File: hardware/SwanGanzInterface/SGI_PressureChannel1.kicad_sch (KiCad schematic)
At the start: 20 parts, among them J6 Conn_01x04_Pin, U10 INA122D, U11 OPA2350

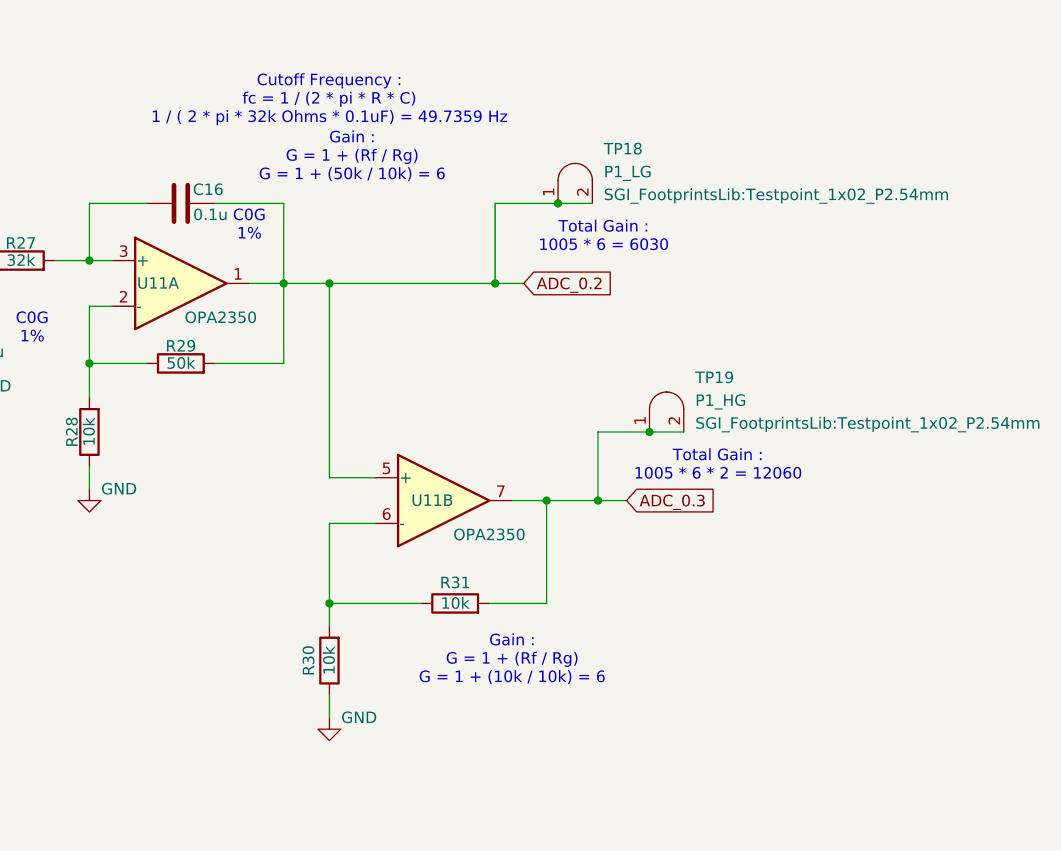
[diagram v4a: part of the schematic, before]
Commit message: Updated Pressure Gain
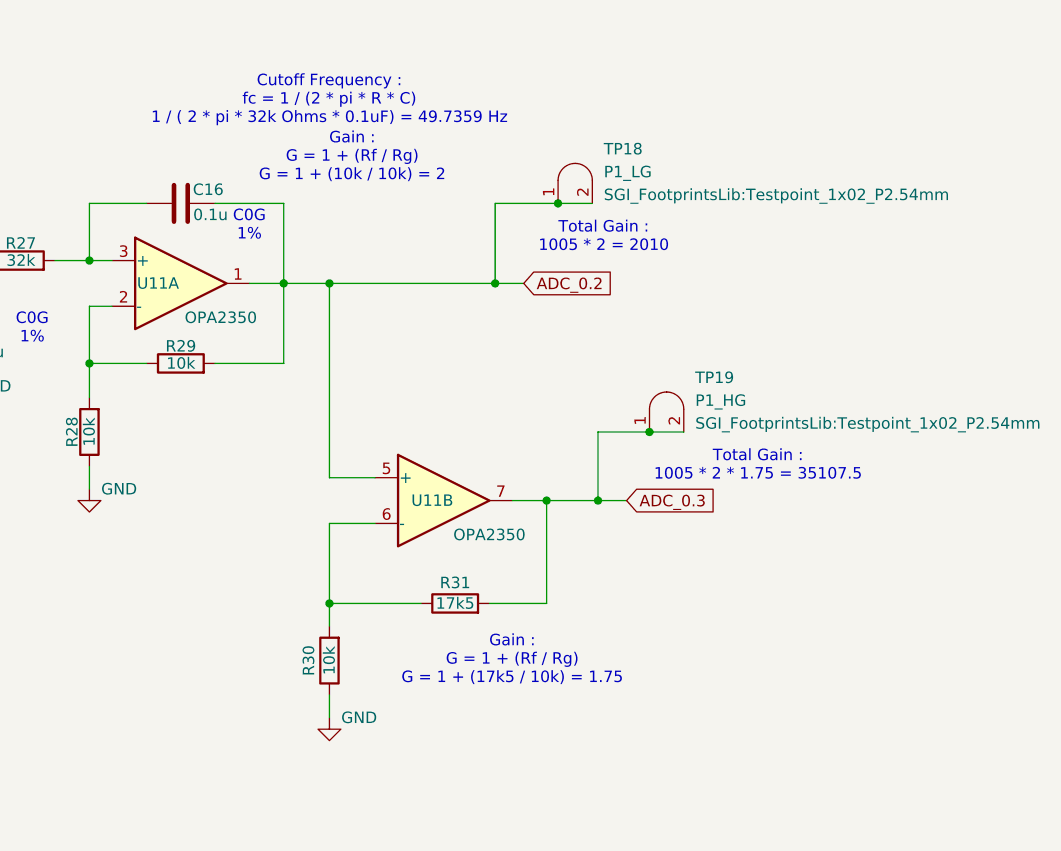
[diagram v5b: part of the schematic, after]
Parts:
- R29: value 50k -> 10k
- R31: value 10k -> 17k5
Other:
- note added: "Gain : G = 1 + (Rf / Rg) G = 1 + (10k / 10k) = 2"
- note added: "Gain : G = 1 + (Rf / Rg) G = 1 + (17k5 / 10k) = 1.75"
- note added: "Total Gain : 1005 * 2 * 1.75 = 35107.5"
- note added: "Total Gain : 1005 * 2 = 2010"
- note removed: "Gain : G = 1 + (Rf / Rg) G = 1 + (10k / 10k) = 6"
- note removed: "Gain : G = 1 + (Rf / Rg) G = 1 + (50k / 10k) = 6"
- note removed: "Total Gain : 1005 * 6 * 2 = 12060"
- note removed: "Total Gain : 1005 * 6 = 6030"
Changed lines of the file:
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@@
 		(comment 3 "Faculty Mentor - Dr. Valvano")
 	)
-	(text "Gain :\nG = 1 + (Rf / Rg)\nG = 1 + (10k / 10k) = 6"
+	(text "Gain :\nG = 1 + (Rf / Rg)\nG = 1 + (17k5 / 10k) = 1.75"
 		(exclude_from_sim no)
 		(at 166.37 106.68 0)
@@
 		)
 	)
-	(text "Total Gain :\n1005 * 6 = 6030"
+	(text "Total Gain :\n1005 * 2 = 2010"
 		(exclude_from_sim no)
 		(at 176.53 59.69 0)
@@
 		)
 	)
-	(text "Gain :\nG = 1 + (Rf / Rg)\nG = 1 + (50k / 10k) = 6"
+	(text "Gain :\nG = 1 + (Rf / Rg)\nG = 1 + (10k / 10k) = 2"
 		(exclude_from_sim no)
 		(at 148.59 50.8 0)
@@
 		)
 	)
-	(text "Total Gain :\n1005 * 6 * 2 = 12060"
-		(exclude_from_sim no)
-		(at 189.23 85.09 0)
+	(text "Total Gain :\n1005 * 2 * 1.75 = 35107.5"
+		(exclude_from_sim no)
+		(at 193.675 85.09 0)
 		(effects
 			(font
@@
 			)
 		)
-		(property "Value" "50k"
+		(property "Value" "10k"
 			(at 129.54 73.66 90)
 			(effects
@@
 			)
 		)
-		(property "Value" "10k"
+		(property "Value" "17k5"
 			(at 160.02 100.33 90)
 			(effects

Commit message: Started Routing
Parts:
- removed TP16, TP17: TP, SGI_FootprintsLib:Testpoint_1x02_P2.54mm, symbol SGI_SymbolLib:Testpoint
- J4: footprint (none) -> SGI_FootprintsLib:Pressure_Connector
- TP15: value TP -> P1_InstOut
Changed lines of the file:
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@@
 	)
 	(junction
-		(at 45.72 134.62)
-		(diameter 0)
-		(color 0 0 0 0)
-	)
-	(junction
 		(at 40.64 59.69)
 		(diameter 0)
@@
 	)
 	(junction
-		(at 45.72 142.24)
-		(diameter 0)
-		(color 0 0 0 0)
-	)
-	(junction
 		(at 164.465 64.77)
 		(diameter 0)
@@
 	(wire
 		(pts
-			(xy 45.72 134.62) (xy 49.53 134.62)
-		)
-		(stroke
-			(width 0)
-			(type default)
-		)
-	)
-	(wire
-		(pts
 			(xy 275.59 49.53) (xy 262.89 49.53)
 		)
@@
 	(wire
 		(pts
-			(xy 39.37 142.24) (xy 45.72 142.24)
-		)
-		(stroke
-			(width 0)
-			(type default)
-		)
-	)
-	(wire
-		(pts
 			(xy 146.05 86.36) (xy 146.05 64.77)
 		)
@@
 	(wire
 		(pts
-			(xy 40.64 134.62) (xy 45.72 134.62)
-		)
-		(stroke
-			(width 0)
-			(type default)
-		)
-	)
-	(wire
-		(pts
 			(xy 275.59 34.29) (xy 275.59 26.67)
 		)
@@
 	(wire
 		(pts
-			(xy 45.72 142.24) (xy 49.53 142.24)
-		)
-		(stroke
-			(width 0)
-			(type default)
-		)
-	)
-	(wire
-		(pts
 			(xy 140.97 64.77) (xy 137.16 64.77)
 		)
@@
 		)
 	)
-	(global_label "Pres1AmpOut_LowGain"
-		(shape input)
-		(at 40.64 134.62 180)
-		(fields_autoplaced yes)
-		(effects
-			(font
-				(size 1.27 1.27)
-			)
-			(justify right)
-		)
-		(property "Intersheetrefs" "${INTERSHEET_REFS}"
-			(at 16.4883 134.62 0)
-			(effects
-				(font
-					(size 1.27 1.27)
-				)
-				(justify right)
-				(hide yes)
-			)
-		)
-	)
 	(global_label "P1__InstrOut"
 		(shape input)
@@
 		)
 	)
-	(global_label "Pres1AmpOut_HighGain"
-		(shape input)
-		(at 39.37 142.24 180)
-		(fields_autoplaced yes)
-		(effects
-			(font
-				(size 1.27 1.27)
-			)
-			(justify right)
-		)
-		(property "Intersheetrefs" "${INTERSHEET_REFS}"
-			(at 14.4926 142.24 0)
-			(effects
-				(font
-					(size 1.27 1.27)
-				)
-				(justify right)
-				(hide yes)
-			)
-		)
-	)
-	(symbol
-		(lib_id "SGI_SymbolLib:Testpoint")
-		(at 47.625 134.62 0)
-		(unit 1)
-		(exclude_from_sim no)
-		(in_bom yes)
-		(on_board yes)
-		(dnp no)
-		(fields_autoplaced yes)
-		(property "Reference" "TP16"
-			(at 51.181 128.5873 0)
-			(effects
-				(font
-					(size 1.27 1.27)
-				)
-				(justify left)
-			)
-		)
-		(property "Value" "TP"
-			(at 51.181 131.1273 0)
-			(effects
-				(font
-					(size 1.27 1.27)
-				)
-				(justify left)
-			)
-		)
-		(property "Footprint" "SGI_FootprintsLib:Testpoint_1x02_P2.54mm"
-			(at 51.181 133.6673 0)
-			(effects
-				(font
-					(size 1.27 1.27)
-				)
-				(justify left)
-			)
-		)
-		(property "Datasheet" "~"
-			(at 47.625 134.62 0)
-			(effects
-				(font
-					(size 1.27 1.27)
-				)
-				(hide yes)
-			)
-		)
-		(property "Description" "Testpoint"
-			(at 47.625 134.62 0)
-			(effects
-				(font
-					(size 1.27 1.27)
-				)
-				(hide yes)
-			)
-		)
-		(pin "2"
-		)
-		(pin "1"
-		)
-		(instances
-			(project "SwanGanzInterface"
-				(path "/4e9a6e30-f660-472b-9696-bea1f34b4545/3d8fa9e7-4833-4941-a955-d778effe3e32"
-					(reference "TP16")
-					(unit 1)
-				)
-			)
-		)
-	)
 	(symbol
 		(lib_id "power:GNDA")
@@
 		(fields_autoplaced yes)
 		(property "Reference" "TP15"
-			(at 51.181 120.9673 0)
+			(at 50.8 120.9673 0)
 			(effects
 				(font
@@
 			)
 		)
-		(property "Value" "TP"
-			(at 51.181 123.5073 0)
+		(property "Value" "P1_InstOut"
+			(at 50.8 123.5073 0)
 			(effects
 				(font
@@
 		)
 		(property "Footprint" "SGI_FootprintsLib:Testpoint_1x02_P2.54mm"
-			(at 51.181 126.0473 0)
+			(at 50.8 126.0473 0)
 			(effects
 				(font
@@
 			)
 		)
-		(property "Footprint" ""
+		(property "Footprint" "SGI_FootprintsLib:Pressure_Connector"
 			(at 24.13 62.23 0)
 			(effects
@@
 	)
 	(symbol
-		(lib_id "SGI_SymbolLib:Testpoint")
-		(at 47.625 142.24 0)
-		(unit 1)
-		(exclude_from_sim no)
-		(in_bom yes)
-		(on_board yes)
-		(dnp no)
-		(fields_autoplaced yes)
-		(property "Reference" "TP17"
-			(at 51.181 136.2073 0)
-			(effects
-				(font
-					(size 1.27 1.27)
-				)
-				(justify left)
-			)
-		)
-		(property "Value" "TP"
-			(at 51.181 138.7473 0)
-			(effects
-				(font
-					(size 1.27 1.27)
-				)
-				(justify left)
-			)
-		)
-		(property "Footprint" "SGI_FootprintsLib:Testpoint_1x02_P2.54mm"
-			(at 51.181 141.2873 0)
-			(effects
-				(font
-					(size 1.27 1.27)
-				)
-				(justify left)
-			)
-		)
-		(property "Datasheet" "~"
-			(at 47.625 142.24 0)
-			(effects
-				(font
-					(size 1.27 1.27)
-				)
-				(hide yes)
-			)
-		)
-		(property "Description" "Testpoint"
-			(at 47.625 142.24 0)
-			(effects
-				(font
-					(size 1.27 1.27)
-				)
-				(hide yes)
-			)
-		)
-		(pin "2"
-		)
-		(pin "1"
-		)
-		(instances
-			(project "SwanGanzInterface"
-				(path "/4e9a6e30-f660-472b-9696-bea1f34b4545/3d8fa9e7-4833-4941-a955-d778effe3e32"
-					(reference "TP17")
-					(unit 1)
-				)
-			)
-		)
-	)
-	(symbol
 		(lib_id "Device:R")
 		(at 97.79 62.23 90)
@@
 			)
 		)
-		(property "Footprint" ""
+		(property "Footprint" "SGI_FootprintsLib:Pressure_Connector"
 			(at 24.13 99.06 0)
 			(effects

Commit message: Reannotated symbols
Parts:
- renumbered J6 to J5, TP15 to TP10, TP18 to TP11, TP19 to TP12
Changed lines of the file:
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@@
 		(on_board yes)
 		(dnp no)
-		(property "Reference" "#PWR059"
+		(property "Reference" "#PWR057"
 			(at 146.05 119.38 0)
 			(effects
@@
 			(project "SwanGanzInterface"
 				(path "/4e9a6e30-f660-472b-9696-bea1f34b4545/3d8fa9e7-4833-4941-a955-d778effe3e32"
-					(reference "#PWR059")
+					(reference "#PWR057")
 					(unit 1)
 				)
@@
 		(dnp no)
 		(fields_autoplaced yes)
-		(property "Reference" "#PWR055"
+		(property "Reference" "#PWR053"
 			(at 74.93 46.99 0)
 			(effects
@@
 			(project "SwanGanzInterface"
 				(path "/4e9a6e30-f660-472b-9696-bea1f34b4545/3d8fa9e7-4833-4941-a955-d778effe3e32"
-					(reference "#PWR055")
+					(reference "#PWR053")
 					(unit 1)
 				)
@@
 		(on_board yes)
 		(dnp no)
-		(property "Reference" "#PWR057"
+		(property "Reference" "#PWR055"
 			(at 105.41 82.55 0)
 			(effects
@@
 			(project "SwanGanzInterface"
 				(path "/4e9a6e30-f660-472b-9696-bea1f34b4545/3d8fa9e7-4833-4941-a955-d778effe3e32"
-					(reference "#PWR057")
+					(reference "#PWR055")
 					(unit 1)
 				)
@@
 		(dnp no)
 		(fields_autoplaced yes)
-		(property "Reference" "J6"
+		(property "Reference" "J5"
 			(at 26.035 177.8 0)
 			(effects
@@
 			(project ""
 				(path "/4e9a6e30-f660-472b-9696-bea1f34b4545/3d8fa9e7-4833-4941-a955-d778effe3e32"
-					(reference "J6")
+					(reference "J5")
 					(unit 1)
 				)
@@
 		(on_board yes)
 		(dnp no)
-		(property "Reference" "#PWR054"
+		(property "Reference" "#PWR052"
 			(at 62.23 88.9 0)
 			(effects
@@
 			(project "SwanGanzInterface"
 				(path "/4e9a6e30-f660-472b-9696-bea1f34b4545/3d8fa9e7-4833-4941-a955-d778effe3e32"
-					(reference "#PWR054")
+					(reference "#PWR052")
 					(unit 1)
 				)
@@
 		(on_board yes)
 		(dnp no)
-		(property "Reference" "#PWR072"
+		(property "Reference" "#PWR049"
 			(at 35.56 199.39 0)
 			(effects
@@
 			(project "SwanGanzInterface"
 				(path "/4e9a6e30-f660-472b-9696-bea1f34b4545/3d8fa9e7-4833-4941-a955-d778effe3e32"
-					(reference "#PWR072")
+					(reference "#PWR049")
 					(unit 1)
 				)
@@
 		(on_board yes)
 		(dnp no)
-		(property "Reference" "#PWR058"
+		(property "Reference" "#PWR056"
 			(at 119.38 93.98 0)
 			(effects
@@
 			(project "SwanGanzInterface"
 				(path "/4e9a6e30-f660-472b-9696-bea1f34b4545/3d8fa9e7-4833-4941-a955-d778effe3e32"
-					(reference "#PWR058")
+					(reference "#PWR056")
 					(unit 1)
 				)
@@
 		(dnp no)
 		(fields_autoplaced yes)
-		(property "Reference" "#PWR061"
+		(property "Reference" "#PWR059"
 			(at 262.89 58.42 0)
 			(effects
@@
 			(project "SwanGanzInterface"
 				(path "/4e9a6e30-f660-472b-9696-bea1f34b4545/3d8fa9e7-4833-4941-a955-d778effe3e32"
-					(reference "#PWR061")
+					(reference "#PWR059")
 					(unit 1)
 				)
@@
 		(dnp no)
 		(fields_autoplaced yes)
-		(property "Reference" "TP15"
+		(property "Reference" "TP10"
 			(at 50.8 120.9673 0)
 			(effects
@@
 			(project "SwanGanzInterface"
 				(path "/4e9a6e30-f660-472b-9696-bea1f34b4545/3d8fa9e7-4833-4941-a955-d778effe3e32"
-					(reference "TP15")
+					(reference "TP10")
 					(unit 1)
 				)
@@
 		(on_board yes)
 		(dnp no)
-		(property "Reference" "#PWR053"
+		(property "Reference" "#PWR051"
 			(at 62.23 39.37 0)
 			(effects
@@
 			(project "SwanGanzInterface"
 				(path "/4e9a6e30-f660-472b-9696-bea1f34b4545/3d8fa9e7-4833-4941-a955-d778effe3e32"
-					(reference "#PWR053")
+					(reference "#PWR051")
 					(unit 1)
 				)
@@
 		(dnp no)
 		(fields_autoplaced yes)
-		(property "Reference" "TP18"
+		(property "Reference" "TP11"
 			(at 176.53 49.8473 0)
 			(effects
@@
 			(project "SwanGanzInterface"
 				(path "/4e9a6e30-f660-472b-9696-bea1f34b4545/3d8fa9e7-4833-4941-a955-d778effe3e32"
-					(reference "TP18")
+					(reference "TP11")
 					(unit 1)
 				)
@@
 		(dnp no)
 		(fields_autoplaced yes)
-		(property "Reference" "TP19"
+		(property "Reference" "TP12"
 			(at 186.69 75.2473 0)
 			(effects
@@
 			(project "SwanGanzInterface"
 				(path "/4e9a6e30-f660-472b-9696-bea1f34b4545/3d8fa9e7-4833-4941-a955-d778effe3e32"
-					(reference "TP19")
+					(reference "TP12")
 					(unit 1)
 				)
@@
 		(on_board yes)
 		(dnp no)
-		(property "Reference" "#PWR052"
+		(property "Reference" "#PWR050"
 			(at 36.83 78.74 0)
 			(effects
@@
 			(project "SwanGanzInterface"
 				(path "/4e9a6e30-f660-472b-9696-bea1f34b4545/3d8fa9e7-4833-4941-a955-d778effe3e32"
-					(reference "#PWR052")
+					(reference "#PWR050")
 					(unit 1)
 				)
@@
 		(on_board yes)
 		(dnp no)
-		(property "Reference" "#PWR056"
+		(property "Reference" "#PWR054"
 			(at 74.93 83.82 0)
 			(effects
@@
 			(project "SwanGanzInterface"
 				(path "/4e9a6e30-f660-472b-9696-bea1f34b4545/3d8fa9e7-4833-4941-a955-d778effe3e32"
-					(reference "#PWR056")
+					(reference "#PWR054")
 					(unit 1)
 				)
@@
 		(on_board yes)
 		(dnp no)
-		(property "Reference" "#PWR060"
+		(property "Reference" "#PWR058"
 			(at 262.89 27.94 0)
 			(effects
@@
 			(project "SwanGanzInterface"
 				(path "/4e9a6e30-f660-472b-9696-bea1f34b4545/3d8fa9e7-4833-4941-a955-d778effe3e32"
-					(reference "#PWR060")
-					(unit 1)
-				)
+					(reference "#PWR058")
+					(unit 1)
+				)

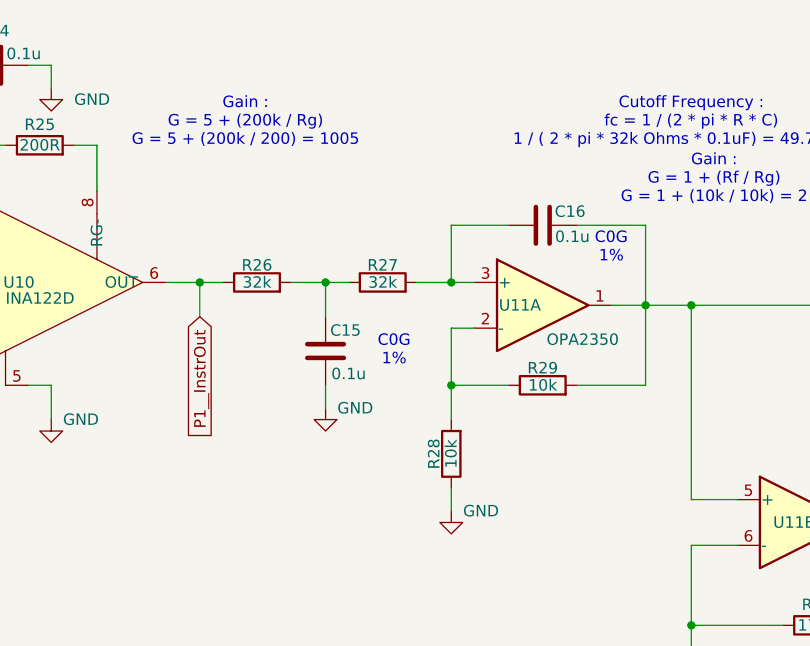
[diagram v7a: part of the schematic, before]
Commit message: Fixed butterworth filters
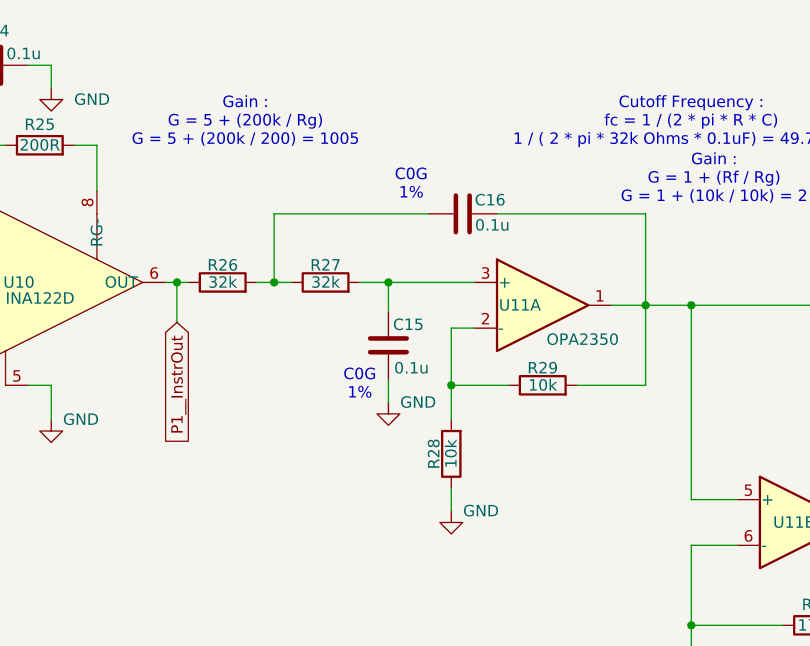
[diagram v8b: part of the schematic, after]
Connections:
- net at R26.2, R27.1: now also C16.1; no longer C15.1
- net at R27.2, U11.3 (+): now also C15.1; no longer C16.1
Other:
- moved on the sheet: C15, C16, R26, R27
